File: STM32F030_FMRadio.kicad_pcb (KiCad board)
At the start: 2 copper layers, 77 x 15 mm, 17 parts, among them J1 Conn_01x04_Female, J2 Screw_Terminal_01x02, J3 AudioJack3_Ground, SW1 Rotary_Encoder_Switch, U1 LP5907MFX-3.3, U2 STM32F030F4Px, U3 TEA5767

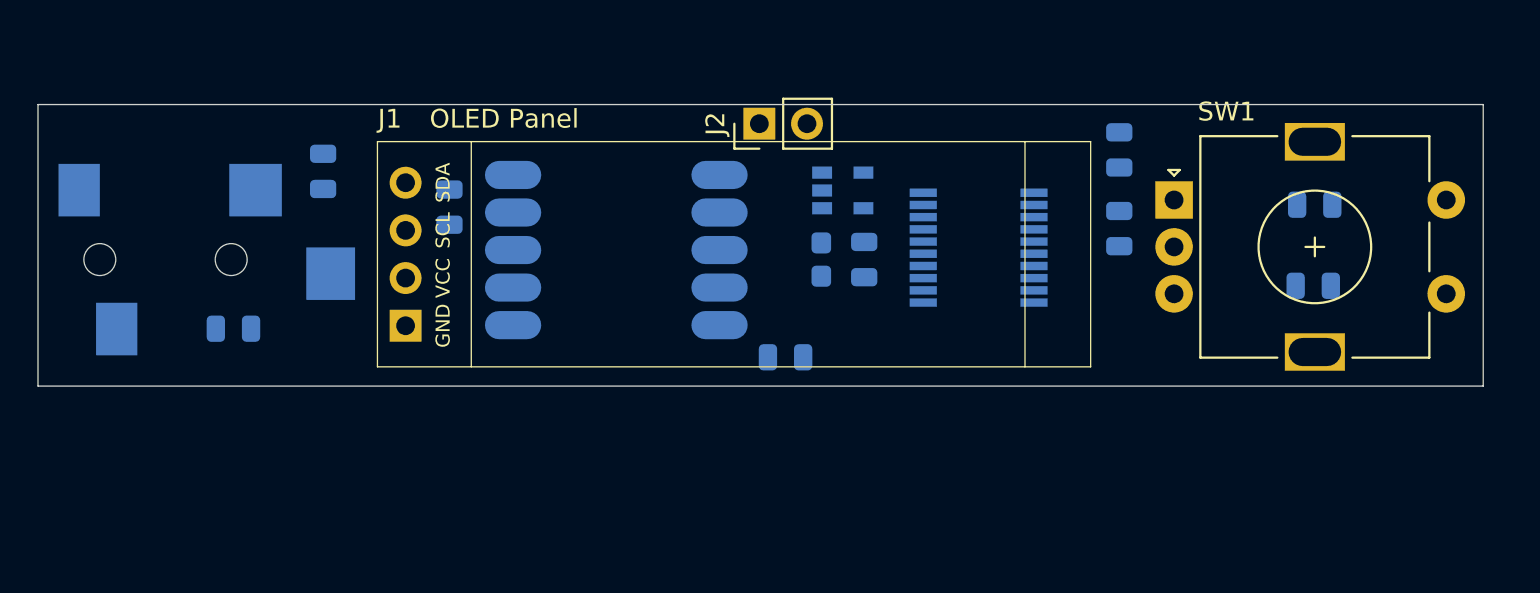
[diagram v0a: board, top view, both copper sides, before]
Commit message: + pull_Up encoder, разведена ПП
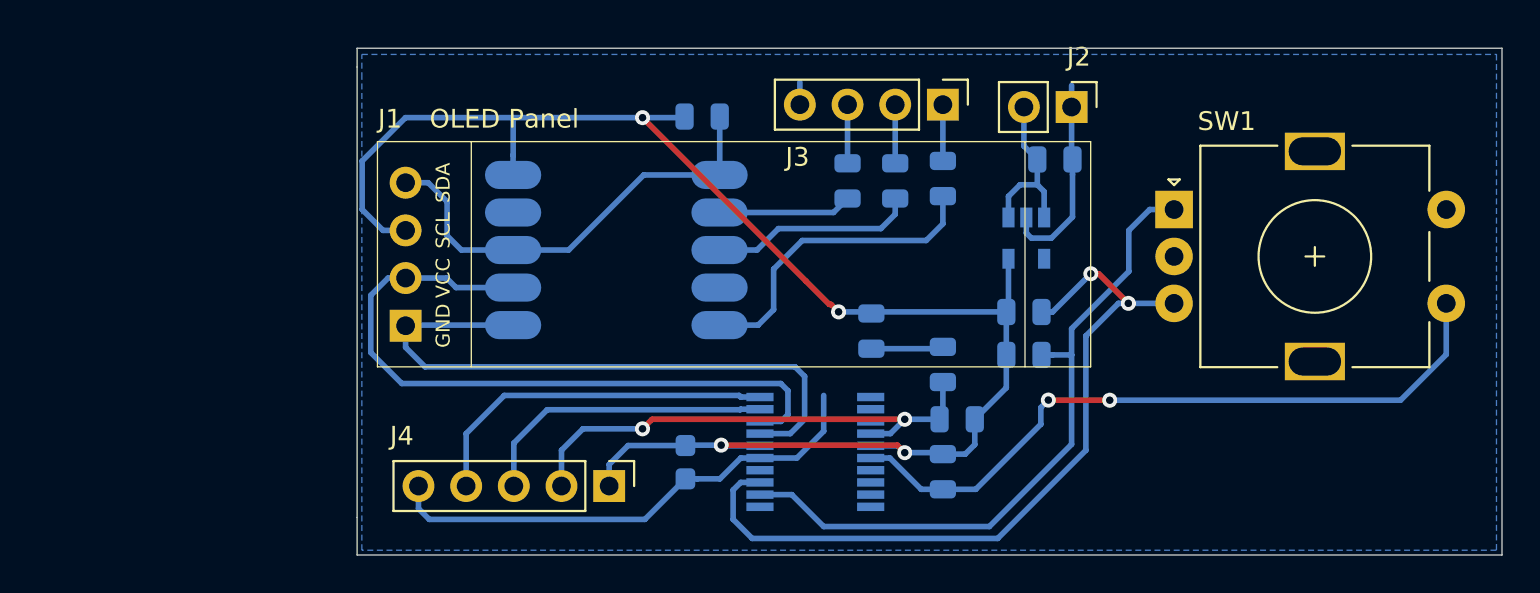
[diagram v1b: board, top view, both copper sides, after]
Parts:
- added J4: Conn_01x05, Connector_PinHeader_2.54mm:PinHeader_1x05_P2.54mm_Vertical, F.Cu at (146.4, 60.3)
- added R3: R, Resistor_SMD:R_0805_2012Metric, B.Cu at (168.5, 53.3)
- added R4: R, Resistor_SMD:R_0805_2012Metric, B.Cu at (168.5, 51.1)
- J3: value AudioJack3_Ground -> Conn_01x04; footprint Connector_Audio:Jack_3.5mm_CUI_SJ-3524-SMT_Horizontal -> Connector_PinHeader_2.54mm:PinHeader_1x04_P2.54mm_Vertical; moved to F.Cu
- moved J3 43.2 mm to (164.2, 40.0)
- moved C7 33.7 mm to (159.1, 44.1), turned to 270 degrees
- moved C6 30.5 mm to (161.7, 44.1), turned to 270 degrees
- moved R2 22.1 mm to (164.2, 59.6), turned to 90 degrees
- moved R1 16.7 mm to (165.0, 56.8), turned to 180 degrees
- moved J2 16.7 mm to (171.1, 40.1), turned to 270 degrees
- moved C5 14.3 mm to (151.4, 40.6), turned to 0 degrees
- moved C1 14.1 mm to (170.2, 42.9)
- moved U2 13.9 mm to (157.4, 58.5)
- moved C2 13.0 mm to (150.5, 59.1)
- moved C8 12.7 mm to (164.2, 43.9), turned to 270 degrees
- moved C4 11.9 mm to (164.2, 53.8), turned to 90 degrees
- moved U1 10.1 mm to (168.7, 47.1), turned to 270 degrees
- moved C3 3.83 mm to (160.4, 52.1)
- moved SW1 0.51 mm to (176.5, 45.6)
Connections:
- net Net-(C1-Pad1) renamed /VCC
- net Net-(C4-Pad1) renamed /NRST
- U2 pad 19: Net-(U2-Pad19) -> /SWDIO
- U2 pad 20: Net-(U2-Pad20) -> /SWCLK
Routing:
- net /+3V3: track 0.00 -> 86.5 mm, vias 0 -> 4
- net GND: track 0.00 -> 66.9 mm
- net Net-(R4-Pad1): track 0.00 -> 42.0 mm, vias 0 -> 2
- net Net-(R2-Pad1): track 0.00 -> 37.6 mm, vias 0 -> 2
- net /SCL: track 0.00 -> 37.2 mm
- net Net-(R3-Pad1): track 0.00 -> 36.3 mm
- net /SDA: track 0.00 -> 33.8 mm
- net /NRST: track 0.00 -> 26.9 mm, vias 0 -> 2
- net /SWCLK: track 0.00 -> 19.3 mm
- net Net-(C8-Pad2): track 0.00 -> 16.9 mm
- net /SWDIO: track 0.00 -> 16.1 mm
- net Net-(C6-Pad2): track 0.00 -> 11.7 mm
- net /VCC: track 0.00 -> 9.25 mm
- net Net-(C7-Pad2): track 0.00 -> 8.63 mm
- net Net-(C7-Pad1): track 0.00 -> 3.13 mm
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- added copper zone on B.Cu, net GND
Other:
- board size 77 x 15 mm -> 61 x 27 mm

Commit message: малкие правки разводки
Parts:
- moved C1 0.73 mm to (169.4, 42.9)
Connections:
- U1 pad 4: Net-(U1-Pad4) -> GND
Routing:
- net GND: track 66.9 -> 59.8 mm
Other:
- board size 61 x 27 mm -> 62 x 27 mm
